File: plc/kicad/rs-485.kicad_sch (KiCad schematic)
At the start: 10 parts, among them CN11 DB2ERC-5.08-4P, SW5 MSK12C02, U15 THVD1450DR

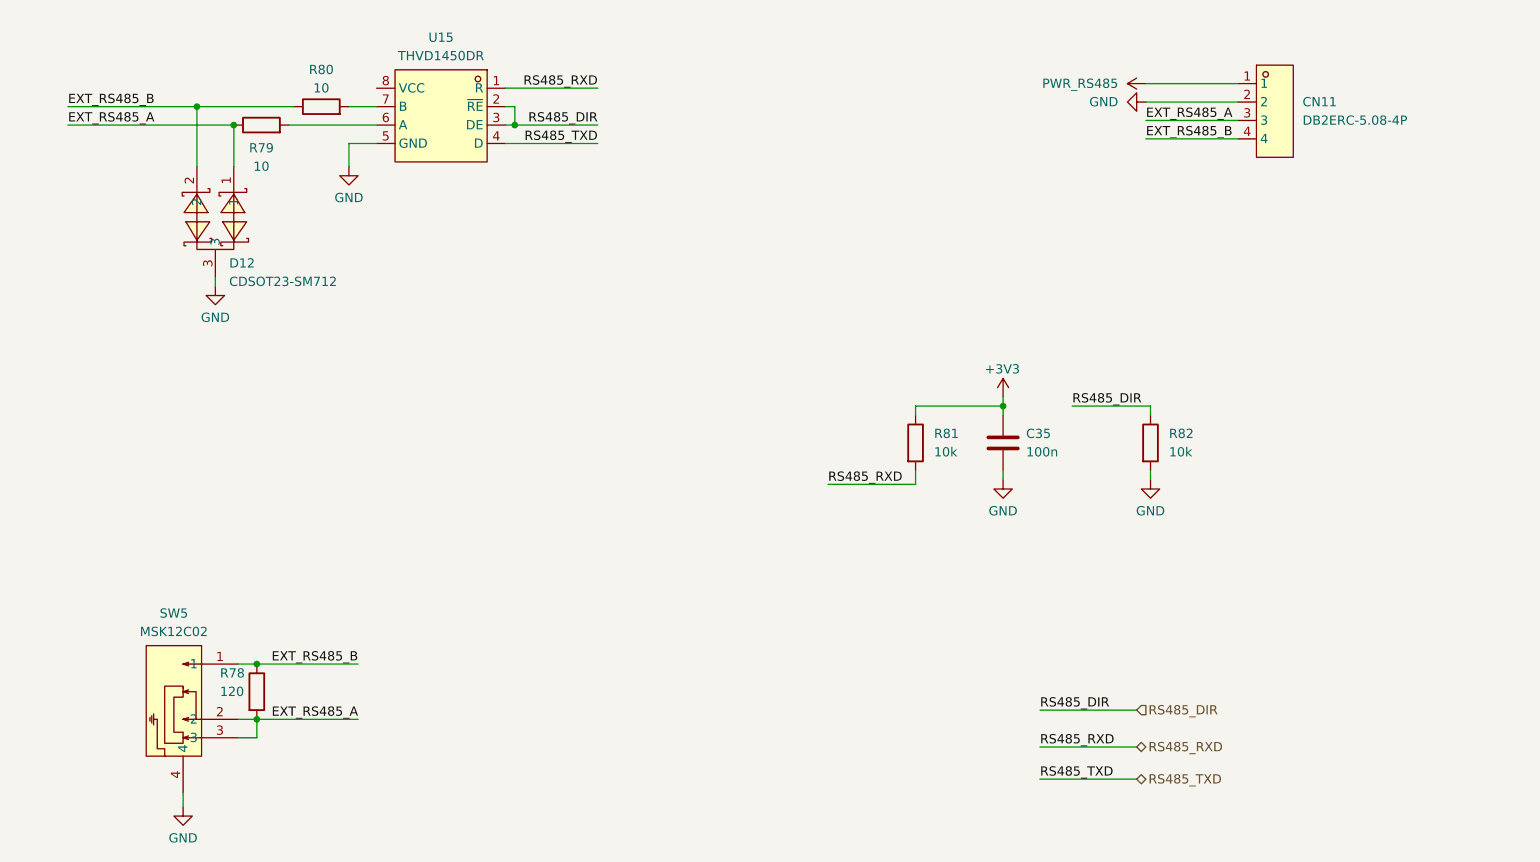
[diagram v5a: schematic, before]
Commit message: AHT20 sensor added
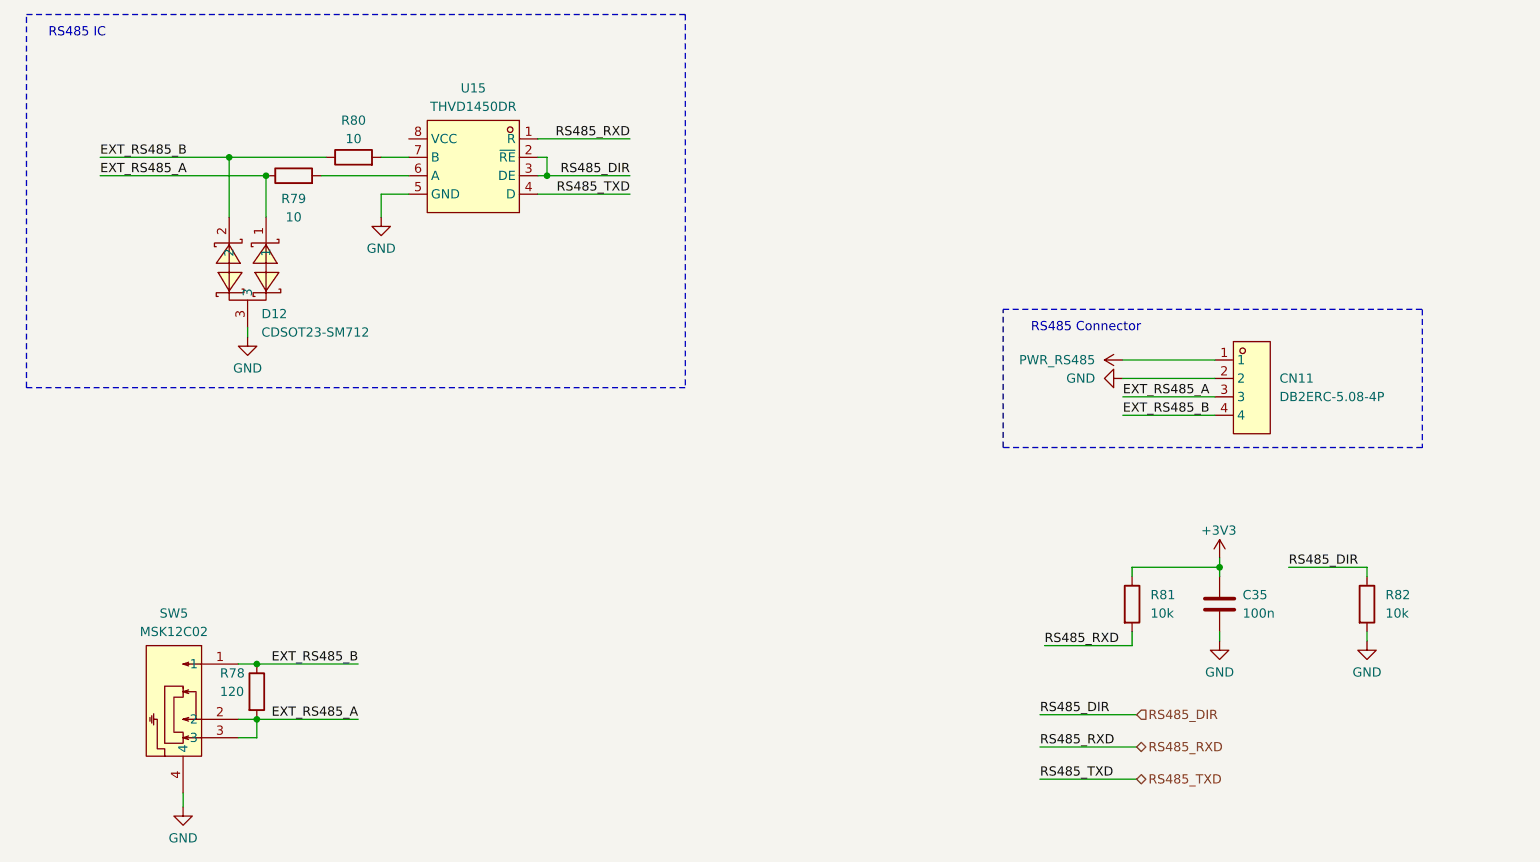
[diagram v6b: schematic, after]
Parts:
- C35: footprint Capacitor_SMD:C_0805_2012Metric -> Capacitor_SMD:C_0603_1608Metric
- R78, R79, R80, R81, R82: footprint Resistor_SMD:R_0805_2012Metric -> Resistor_SMD:R_0603_1608Metric
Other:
- note added: "RS485 Connector"
- note added: "RS485 IC"
- moved on the sheet: C35, CN11, D12, R79, R80, R81, R82, U15

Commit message: PCB placement
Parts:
- renumbered C35 to C42, CN11 to CN12, D12 to D16, R78 to R81, R79 to R82, R80 to R83, R81 to R84, R82 to R85, U15 to U19
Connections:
- net +3V3: now also U19.8 (VCC)
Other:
- title: (none) -> LibrePLC32
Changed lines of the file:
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@@
 	(generator_version "10.0")
 	(paper "A4")
+	(title_block
+		(title "LibrePLC32")
+		(date "2026-04-12")
+		(rev "A")
+	)
 	(rectangle
 		(start 37.465 51.435)
@@
 	(wire
 		(pts
+			(xy 88.265 66.675) (xy 88.265 68.58)
+		)
+		(stroke
+			(width 0)
+			(type default)
+		)
+	)
+	(wire
+		(pts
 			(xy 70.485 73.66) (xy 70.485 79.375)
 		)
@@
 		(pts
 			(xy 189.865 136.525) (xy 189.865 138.43)
+		)
+		(stroke
+			(width 0)
+			(type default)
+		)
+	)
+	(wire
+		(pts
+			(xy 88.265 68.58) (xy 90.17 68.58)
 		)
 		(stroke
@@
 					(size 1.27 1.27)
 					(italic yes)
+				)
+			)
+		)
+	)
+	(symbol
+		(lib_id "power:+3V3")
+		(at 88.265 66.675 0)
+		(unit 1)
+		(body_style 1)
+		(exclude_from_sim no)
+		(in_bom yes)
+		(on_board yes)
+		(in_pos_files yes)
+		(dnp no)
+		(property "Reference" "#PWR0246"
+			(at 88.265 70.485 0)
+			(hide yes)
+			(show_name no)
+			(do_not_autoplace no)
+			(effects
+				(font
+					(size 1.27 1.27)
+				)
+			)
+		)
+		(property "Value" "+3V3"
+			(at 85.725 62.865 0)
+			(show_name no)
+			(do_not_autoplace no)
+			(effects
+				(font
+					(size 1.27 1.27)
+				)
+				(justify left)
+			)
+		)
+		(property "Footprint" ""
+			(at 88.265 66.675 0)
+			(hide yes)
+			(show_name no)
+			(do_not_autoplace no)
+			(effects
+				(font
+					(size 1.27 1.27)
+				)
+			)
+		)
+		(property "Datasheet" ""
+			(at 88.265 66.675 0)
+			(hide yes)
+			(show_name no)
+			(do_not_autoplace no)
+			(effects
+				(font
+					(size 1.27 1.27)
+				)
+			)
+		)
+		(property "Description" "Power symbol creates a global label with name \"+3V3\""
+			(at 88.265 66.675 0)
+			(hide yes)
+			(show_name no)
+			(do_not_autoplace no)
+			(effects
+				(font
+					(size 1.27 1.27)
+				)
+			)
+		)
+		(pin "1"
+		)
+		(instances
+			(project "LibrePLC32"
+				(path "/ef4c1a27-85a3-413a-9f93-a41c4f97eee5/58fa1ecb-ea1c-4a70-bb90-31ff9b441562"
+					(reference "#PWR0246")
+					(unit 1)
 				)
 			)
@@
 		(dnp no)
 		(fields_autoplaced yes)
-		(property "Reference" "#PWR0171"
+		(property "Reference" "#PWR0208"
 			(at 222.25 144.145 0)
 			(hide yes)
@@
 			(project "LibrePLC32"
 				(path "/ef4c1a27-85a3-413a-9f93-a41c4f97eee5/58fa1ecb-ea1c-4a70-bb90-31ff9b441562"
-					(reference "#PWR0171")
+					(reference "#PWR0208")
 					(unit 1)
 				)
@@
 		(dnp no)
 		(fields_autoplaced yes)
-		(property "Reference" "#PWR0166"
+		(property "Reference" "#PWR0203"
 			(at 86.36 85.725 0)
 			(hide yes)
@@
 			(project "LibrePLC32"
 				(path "/ef4c1a27-85a3-413a-9f93-a41c4f97eee5/58fa1ecb-ea1c-4a70-bb90-31ff9b441562"
-					(reference "#PWR0166")
+					(reference "#PWR0203")
 					(unit 1)
 				)
@@
 		(dnp no)
 		(fields_autoplaced yes)
-		(property "Reference" "R82"
+		(property "Reference" "R85"
 			(at 224.79 131.4449 0)
 			(show_name no)
@@
 			(project "LibrePLC32"
 				(path "/ef4c1a27-85a3-413a-9f93-a41c4f97eee5/58fa1ecb-ea1c-4a70-bb90-31ff9b441562"
-					(reference "R82")
+					(reference "R85")
 					(unit 1)
 				)
@@
 		(in_pos_files yes)
 		(dnp no)
-		(property "Reference" "D12"
+		(property "Reference" "D16"
 			(at 69.85 92.71 0)
 			(show_name no)
@@
 			(project "LibrePLC32"
 				(path "/ef4c1a27-85a3-413a-9f93-a41c4f97eee5/58fa1ecb-ea1c-4a70-bb90-31ff9b441562"
-					(reference "D12")
+					(reference "D16")
 					(unit 1)
 				)
@@
 		(in_pos_files yes)
 		(dnp no)
-		(property "Reference" "R78"
+		(property "Reference" "R81"
 			(at 64.135 142.24 0)
 			(show_name no)
@@
 			(project "LibrePLC32"
 				(path "/ef4c1a27-85a3-413a-9f93-a41c4f97eee5/58fa1ecb-ea1c-4a70-bb90-31ff9b441562"
-					(reference "R78")
+					(reference "R81")
 					(unit 1)
 				)
@@
 		(in_pos_files yes)
 		(dnp no)
-		(property "Reference" "#PWR0167"
+		(property "Reference" "#PWR0206"
 			(at 201.93 130.175 0)
 			(hide yes)
@@
 			(project "LibrePLC32"
 				(path "/ef4c1a27-85a3-413a-9f93-a41c4f97eee5/58fa1ecb-ea1c-4a70-bb90-31ff9b441562"
-					(reference "#PWR0167")
+					(reference "#PWR0206")
 					(unit 1)
 				)
@@
 		(in_pos_files yes)
 		(dnp no)
-		(property "Reference" "R80"
+		(property "Reference" "R83"
 			(at 82.55 66.04 90)
 			(show_name no)
@@
 			(project "LibrePLC32"
 				(path "/ef4c1a27-85a3-413a-9f93-a41c4f97eee5/58fa1ecb-ea1c-4a70-bb90-31ff9b441562"
-					(reference "R80")
+					(reference "R83")
 					(unit 1)
 				)
@@
 		(dnp no)
 		(fields_autoplaced yes)
-		(property "Reference" "#PWR0169"
+		(property "Reference" "#PWR0204"
 			(at 192.405 99.06 0)
 			(hide yes)
@@
 			(project "LibrePLC32"
 				(path "/ef4c1a27-85a3-413a-9f93-a41c4f97eee5/58fa1ecb-ea1c-4a70-bb90-31ff9b441562"
-					(reference "#PWR0169")
+					(reference "#PWR0204")
 					(unit 1)
 				)
@@
 		(dnp no)
 		(fields_autoplaced yes)
-		(property "Reference" "CN11"
+		(property "Reference" "CN12"
 			(at 210.185 101.5999 0)
 			(show_name no)
@@
 			(project "LibrePLC32"
 				(path "/ef4c1a27-85a3-413a-9f93-a41c4f97eee5/58fa1ecb-ea1c-4a70-bb90-31ff9b441562"
-					(reference "CN11")
+					(reference "CN12")
 					(unit 1)
 				)
@@
 		(dnp no)
 		(fields_autoplaced yes)
-		(property "Reference" "C35"
+		(property "Reference" "C42"
 			(at 205.105 131.4449 0)
 			(show_name no)
@@
 			(project "LibrePLC32"
 				(path "/ef4c1a27-85a3-413a-9f93-a41c4f97eee5/58fa1ecb-ea1c-4a70-bb90-31ff9b441562"
-					(reference "C35")
+					(reference "C42")
 					(unit 1)
 				)
@@
 		(dnp no)
 		(fields_autoplaced yes)
-		(property "Reference" "#PWR0165"
+		(property "Reference" "#PWR0202"
 			(at 67.945 102.235 0)
 			(hide yes)
@@
 			(project "LibrePLC32"
 				(path "/ef4c1a27-85a3-413a-9f93-a41c4f97eee5/58fa1ecb-ea1c-4a70-bb90-31ff9b441562"
-					(reference "#PWR0165")
+					(reference "#PWR0202")
 					(unit 1)
 				)
@@
 		(in_pos_files yes)
 		(dnp no)
-		(property "Reference" "R79"
+		(property "Reference" "R82"
 			(at 74.295 76.835 90)
 			(show_name no)
@@
 			(project "LibrePLC32"
 				(path "/ef4c1a27-85a3-413a-9f93-a41c4f97eee5/58fa1ecb-ea1c-4a70-bb90-31ff9b441562"
-					(reference "R79")
+					(reference "R82")
 					(unit 1)
 				)
@@
 		(in_pos_files yes)
 		(dnp no)
-		(property "Reference" "U15"
+		(property "Reference" "U19"
 			(at 99.06 61.595 0)
 			(show_name no)
@@
 			(project "LibrePLC32"
 				(path "/ef4c1a27-85a3-413a-9f93-a41c4f97eee5/58fa1ecb-ea1c-4a70-bb90-31ff9b441562"
-					(reference "U15")
+					(reference "U19")
 					(unit 1)
 				)
@@
 		(dnp no)
 		(fields_autoplaced yes)
-		(property "Reference" "#PWR0164"
+		(property "Reference" "#PWR0201"
 			(at 59.055 167.005 0)
 			(hide yes)
@@
 			(project "LibrePLC32"
 				(path "/ef4c1a27-85a3-413a-9f93-a41c4f97eee5/58fa1ecb-ea1c-4a70-bb90-31ff9b441562"
-					(reference "#PWR0164")
+					(reference "#PWR0201")
 					(unit 1)
 				)
@@
 		(dnp no)
 		(fields_autoplaced yes)
-		(property "Reference" "R81"
+		(property "Reference" "R84"
 			(at 192.405 131.4449 0)
 			(show_name no)
@@
 			(project "LibrePLC32"
 				(path "/ef4c1a27-85a3-413a-9f93-a41c4f97eee5/58fa1ecb-ea1c-4a70-bb90-31ff9b441562"
-					(reference "R81")
+					(reference "R84")
 					(unit 1)
 				)
@@
 		(dnp no)
 		(fields_autoplaced yes)
-		(property "Reference" "#PWR0170"
+		(property "Reference" "#PWR0205"
 			(at 182.245 101.6 0)
 			(hide yes)
@@
 			(project "LibrePLC32"
 				(path "/ef4c1a27-85a3-413a-9f93-a41c4f97eee5/58fa1ecb-ea1c-4a70-bb90-31ff9b441562"
-					(reference "#PWR0170")
+					(reference "#PWR0205")
 					(unit 1)
 				)
@@
 		(dnp no)
 		(fields_autoplaced yes)
-		(property "Reference" "#PWR0168"
+		(property "Reference" "#PWR0207"
 			(at 201.93 144.145 0)
 			(hide yes)
@@
 			(project "LibrePLC32"
 				(path "/ef4c1a27-85a3-413a-9f93-a41c4f97eee5/58fa1ecb-ea1c-4a70-bb90-31ff9b441562"
-					(reference "#PWR0168")
+					(reference "#PWR0207")
 					(unit 1)
 				)

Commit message: RS485 circuit reviewed
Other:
- note added: "10 Ohm Resistors: CRCW0603010RJNEAHP"
- note added: "Termination Resistor"
- moved on the sheet: R81, R84, SW5
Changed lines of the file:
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@@
+	)
+	(rectangle
+		(start 37.465 111.125)
+		(end 88.265 151.765)
+		(stroke
+			(width 0)
+			(type dash)
+		)
+		(fill
+			(type none)
+		)
 	)
 	(rectangle
@@
 				(size 1.27 1.27)
 			)
+		)
+	)
+	(text "Termination Resistor"
+		(exclude_from_sim no)
+		(at 48.26 113.03 0)
+		(effects
+			(font
+				(size 1.27 1.27)
+			)
+		)
+	)
+	(text "10 Ohm Resistors:\nCRCW0603010RJNEAHP"
+		(exclude_from_sim no)
+		(at 104.775 99.695 0)
+		(effects
+			(font
+				(size 1.27 1.27)
+			)
+			(justify left)
 		)
 	)
@@
 	)
 	(junction
-		(at 69.215 140.97)
+		(at 68.58 124.46)
 		(diameter 0)
 		(color 0 0 0 0)
@@
 	)
 	(junction
-		(at 69.215 148.59)
+		(at 68.58 132.08)
 		(diameter 0)
 		(color 0 0 0 0)
@@
 	(wire
 		(pts
-			(xy 177.8 138.43) (xy 189.865 138.43)
-		)
-		(stroke
-			(width 0)
-			(type default)
-		)
-	)
-	(wire
-		(pts
-			(xy 59.055 160.655) (xy 59.055 158.75)
+			(xy 179.705 138.43) (xy 191.77 138.43)
+		)
+		(stroke
+			(width 0)
+			(type default)
+		)
+	)
+	(wire
+		(pts
+			(xy 58.42 144.145) (xy 58.42 142.24)
 		)
 		(stroke
@@
 	(wire
 		(pts
-			(xy 189.865 127.635) (xy 189.865 128.905)
+			(xy 191.77 127.635) (xy 191.77 128.905)
 		)
 		(stroke
@@
 	(wire
 		(pts
-			(xy 69.215 151.13) (xy 69.215 148.59)
-		)
-		(stroke
-			(width 0)
-			(type default)
-		)
-	)
-	(wire
-		(pts
-			(xy 69.215 148.59) (xy 83.185 148.59)
+			(xy 68.58 134.62) (xy 68.58 132.08)
+		)
+		(stroke
+			(width 0)
+			(type default)
+		)
+	)
+	(wire
+		(pts
+			(xy 68.58 132.08) (xy 82.55 132.08)
 		)
 		(stroke
@@
 	(wire
 		(pts
-			(xy 66.675 151.13) (xy 69.215 151.13)
-		)
-		(stroke
-			(width 0)
-			(type default)
-		)
-	)
-	(wire
-		(pts
-			(xy 66.675 140.97) (xy 69.215 140.97)
+			(xy 66.04 134.62) (xy 68.58 134.62)
+		)
+		(stroke
+			(width 0)
+			(type default)
+		)
+	)
+	(wire
+		(pts
+			(xy 66.04 124.46) (xy 68.58 124.46)
 		)
 		(stroke
@@
 	(wire
 		(pts
-			(xy 66.675 148.59) (xy 69.215 148.59)
+			(xy 66.04 132.08) (xy 68.58 132.08)
 		)
 		(stroke
@@
 	(wire
 		(pts
-			(xy 189.865 136.525) (xy 189.865 138.43)
+			(xy 191.77 136.525) (xy 191.77 138.43)
 		)
 		(stroke
@@
 	(wire
 		(pts
-			(xy 201.93 127.635) (xy 189.865 127.635)
+			(xy 201.93 127.635) (xy 191.77 127.635)
 		)
 		(stroke
@@
 	(wire
 		(pts
-			(xy 69.215 140.97) (xy 83.185 140.97)
+			(xy 68.58 124.46) (xy 82.55 124.46)
 		)
 		(stroke
@@
 	)
 	(label "EXT_RS485_A"
-		(at 83.185 148.59 180)
+		(at 82.55 132.08 180)
 		(effects
 			(font
@@
 	)
 	(label "EXT_RS485_B"
-		(at 83.185 140.97 180)
+		(at 82.55 124.46 180)
 		(effects
 			(font
@@
 	)
 	(label "RS485_RXD"
-		(at 177.8 138.43 0)
+		(at 179.705 138.43 0)
 		(effects
 			(font
@@
 	(symbol
 		(lib_id "Device:R")
-		(at 69.215 144.78 0)
+		(at 68.58 128.27 0)
 		(unit 1)
 		(body_style 1)
@@
 		(dnp no)
 		(property "Reference" "R81"
-			(at 64.135 142.24 0)
+			(at 63.5 125.73 0)
 			(show_name no)
 			(do_not_autoplace no)
@@
 		)
 		(property "Value" "120"
-			(at 64.135 144.78 0)
+			(at 63.5 128.27 0)
 			(show_name no)
 			(do_not_autoplace no)
@@
 		)
 		(property "Footprint" "Resistor_SMD:R_0603_1608Metric"
-			(at 67.437 144.78 90)
+			(at 66.802 128.27 90)
 			(hide yes)
 			(show_name no)
@@
 		)
 		(property "Datasheet" ""
-			(at 69.215 144.78 0)
+			(at 68.58 128.27 0)
 			(hide yes)
 			(show_name no)
@@
 		)
 		(property "Description" "Resistor"
-			(at 69.215 144.78 0)
+			(at 68.58 128.27 0)
 			(hide yes)
 			(show_name no)
@@
 	(symbol
 		(lib_id "LibrePLC32:MSK12C02")
-		(at 60.325 148.59 270)
+		(at 59.69 132.08 270)
 		(unit 1)
 		(body_style 1)
@@
 		(fields_autoplaced yes)
 		(property "Reference" "SW5"
-			(at 57.785 133.985 90)
+			(at 57.15 117.475 90)
 			(show_name no)
 			(do_not_autoplace no)
@@
 		)
 		(property "Value" "MSK12C02"
-			(at 57.785 136.525 90)
+			(at 57.15 120.015 90)
 			(show_name no)
 			(do_not_autoplace no)
@@
 		)
 		(property "Footprint" "LibrePLC32:SW-TH_MSK12C02"
-			(at 51.435 148.59 0)
+			(at 50.8 132.08 0)
 			(hide yes)
 			(show_name no)
@@
 		)
 		(property "Datasheet" "https://lcsc.com/product-detail/Toggle-Switches_SHOU-HAN-MSK12C02_C431540.html"
-			(at 48.895 148.59 0)
+			(at 48.26 132.08 0)
 			(hide yes)
 			(show_name no)
@@
 		)
 		(property "Description" ""
-			(at 60.325 148.59 0)
+			(at 59.69 132.08 0)
 			(hide yes)
 			(show_name no)
@@
 		)
 		(property "Manufacturer" "SHOU HAN(首韩)"
-			(at 46.355 148.59 0)
+			(at 45.72 132.08 0)
 			(hide yes)
 			(show_name no)
@@
 		)
 		(property "MPN" "MSK12C02"
-			(at 43.815 148.59 0)
+			(at 43.18 132.08 0)
 			(hide yes)
 			(show_name no)
@@
 		)
 		(property "LCSC Part" "C431540"
-			(at 41.275 148.59 0)
+			(at 40.64 132.08 0)
 			(hide yes)
 			(show_name no)
@@
 	(symbol
 		(lib_id "power:GND")
-		(at 59.055 160.655 0)
+		(at 58.42 144.145 0)
 		(unit 1)
 		(body_style 1)
@@
 		(fields_autoplaced yes)
 		(property "Reference" "#PWR0201"
-			(at 59.055 167.005 0)
+			(at 58.42 150.495 0)
 			(hide yes)
 			(show_name no)
@@
 		)
 		(property "Value" "GND"
-			(at 59.055 164.973 0)
+			(at 58.42 148.463 0)
 			(show_name no)
 			(do_not_autoplace no)
@@
 		)
 		(property "Footprint" ""
-			(at 59.055 160.655 0)
+			(at 58.42 144.145 0)
 			(hide yes)
 			(show_name no)
@@
 		)
 		(property "Datasheet" ""
-			(at 59.055 160.655 0)
+			(at 58.42 144.145 0)
 			(hide yes)
 			(show_name no)
@@
 		)
 		(property "Description" "Power symbol creates a global label with name \"GND\" , ground"
-			(at 59.055 160.655 0)
+			(at 58.42 144.145 0)
 			(hide yes)
 			(show_name no)
@@
 	(symbol
 		(lib_id "Device:R")
-		(at 189.865 132.715 0)
+		(at 191.77 132.715 0)
 		(unit 1)
 		(body_style 1)
@@
 		(fields_autoplaced yes)
 		(property "Reference" "R84"
-			(at 192.405 131.4449 0)
+			(at 194.31 131.4449 0)
 			(show_name no)
 			(do_not_autoplace no)
@@
 		)
 		(property "Value" "10k"
-			(at 192.405 133.9849 0)
+			(at 194.31 133.9849 0)
 			(show_name no)
 			(do_not_autoplace no)
@@
 		)
 		(property "Footprint" "Resistor_SMD:R_0603_1608Metric"
-			(at 188.087 132.715 90)
+			(at 189.992 132.715 90)
 			(hide yes)
 			(show_name no)
@@
 		)
 		(property "Datasheet" ""
-			(at 189.865 132.715 0)
+			(at 191.77 132.715 0)
 			(hide yes)
 			(show_name no)
@@
 		)
 		(property "Description" "Resistor"
-			(at 189.865 132.715 0)
-			(hide yes)
-			(show_name no)
+			(at 191.77 132.715 0)
+			(hide yes)
+			(show_name no)
